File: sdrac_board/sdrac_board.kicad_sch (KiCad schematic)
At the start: 9 parts

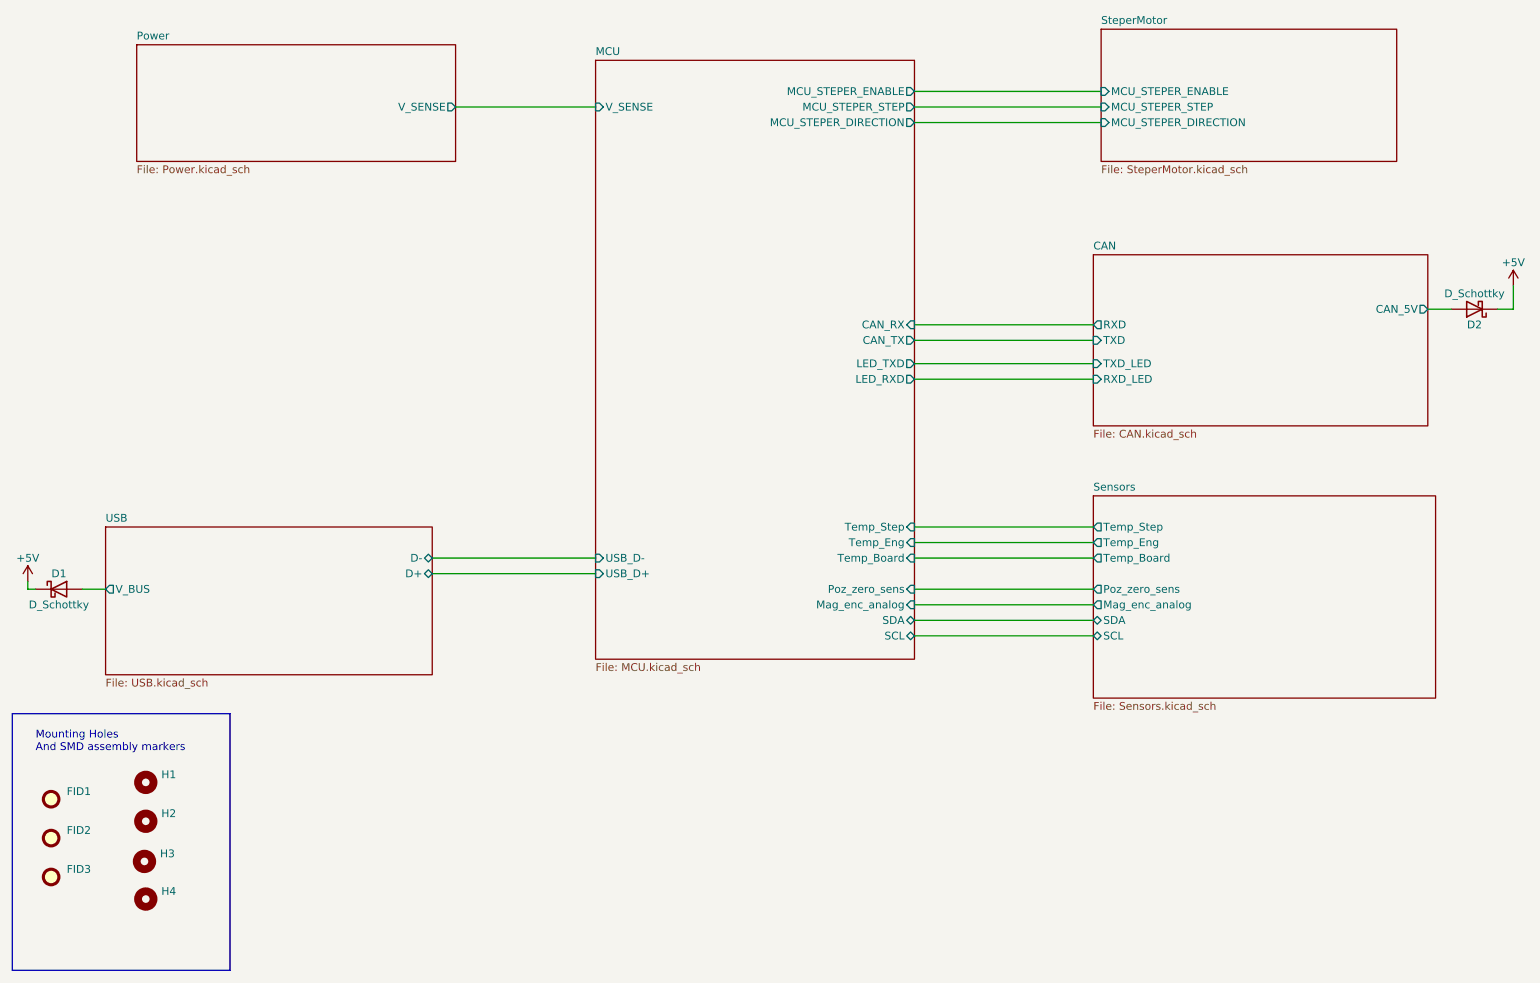
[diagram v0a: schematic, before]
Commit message: added second I2C communscation lane for synchronization and added wyas to change mcirosteping with resistors
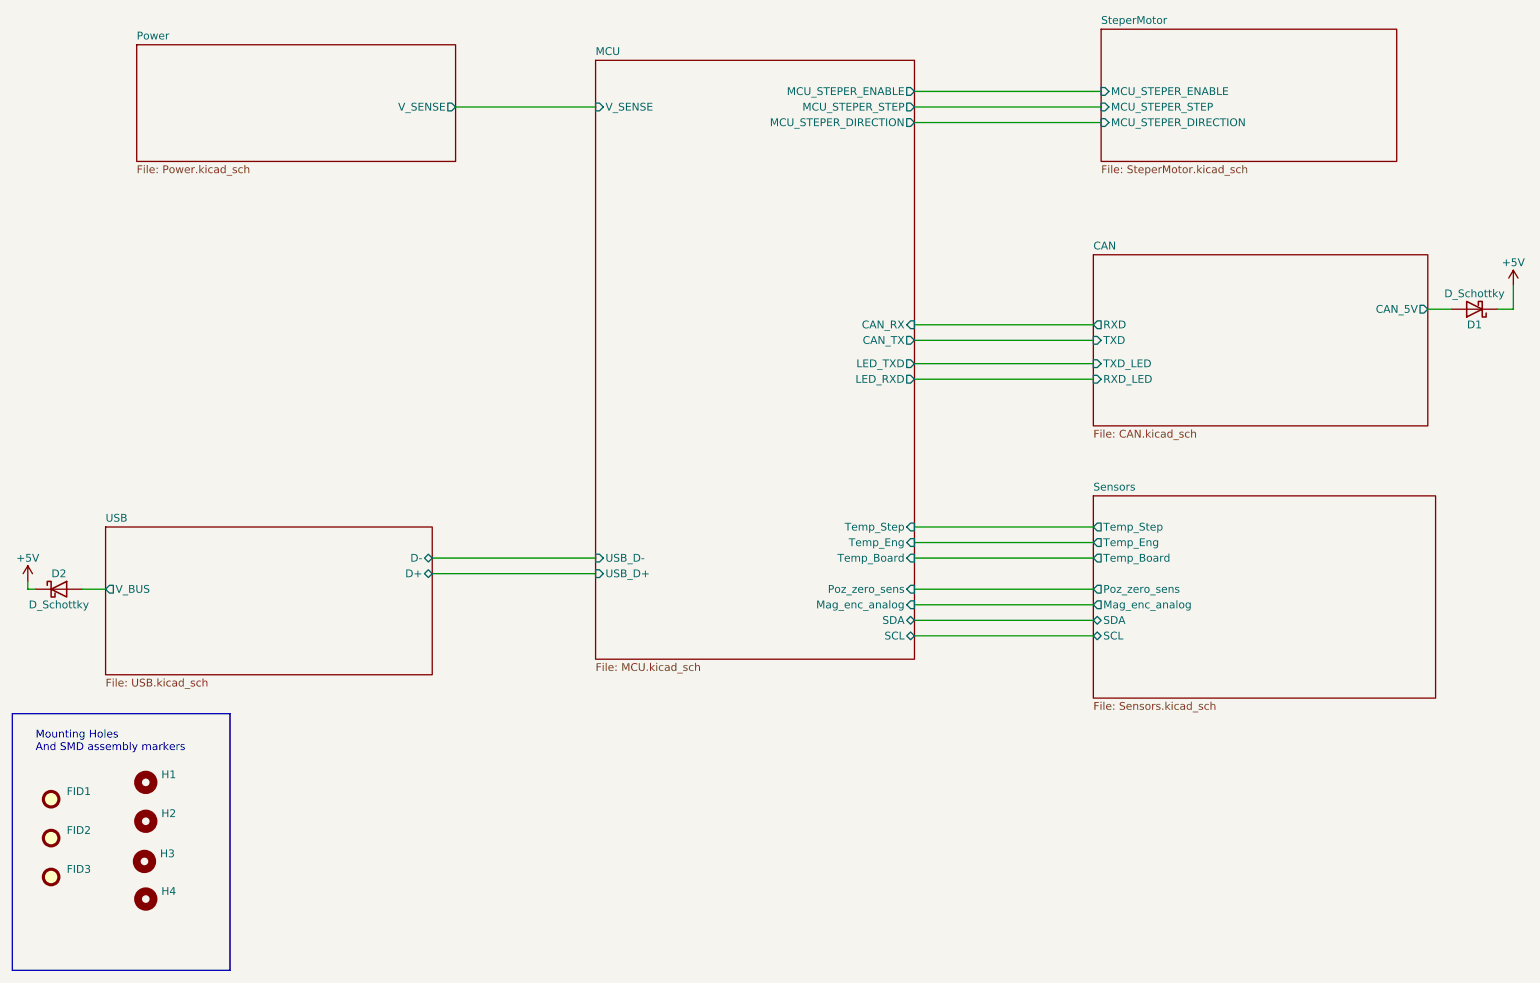
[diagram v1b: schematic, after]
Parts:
- renumbered D2 to D1, D1 to D2
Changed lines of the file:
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@@
   (symbol (lib_id "power:+5V") (at 24.13 128.27 0) (mirror y) (unit 1)
     (in_bom yes) (on_board yes) (dnp no)
-    (property "Reference" "#PWR01" (at 24.13 132.08 0)
+    (property "Reference" "#PWR02" (at 24.13 132.08 0)
       (effects (font (size 1.27 1.27)) hide)
     )
@@
       (project "sdrac_board"
         (path "/7e6d1db5-12f1-49d6-b3bd-d624ec5345e8"
-          (reference "#PWR01") (unit 1)
+          (reference "#PWR02") (unit 1)
         )
       )
@@
   (symbol (lib_id "Device:D_Schottky") (at 260.35 83.82 180) (unit 1)
     (in_bom yes) (on_board yes) (dnp no)
-    (property "Reference" "D2" (at 260.35 86.36 0)
+    (property "Reference" "D1" (at 260.35 86.36 0)
       (effects (font (size 1.27 1.27)))
     )
@@
       (project "sdrac_board"
         (path "/7e6d1db5-12f1-49d6-b3bd-d624ec5345e8"
-          (reference "D2") (unit 1)
+          (reference "D1") (unit 1)
         )
       )
@@
   (symbol (lib_id "Device:D_Schottky") (at 29.21 129.54 0) (unit 1)
     (in_bom yes) (on_board yes) (dnp no)
-    (property "Reference" "D1" (at 29.21 127 0)
+    (property "Reference" "D2" (at 29.21 127 0)
       (effects (font (size 1.27 1.27)))
     )
@@
       (project "sdrac_board"
         (path "/7e6d1db5-12f1-49d6-b3bd-d624ec5345e8"
-          (reference "D1") (unit 1)
+          (reference "D2") (unit 1)
         )
       )
@@
   (symbol (lib_id "power:+5V") (at 266.7 80.01 0) (mirror y) (unit 1)
     (in_bom yes) (on_board yes) (dnp no)
-    (property "Reference" "#PWR02" (at 266.7 83.82 0)
+    (property "Reference" "#PWR01" (at 266.7 83.82 0)
       (effects (font (size 1.27 1.27)) hide)
     )
@@
       (project "sdrac_board"
         (path "/7e6d1db5-12f1-49d6-b3bd-d624ec5345e8"
-          (reference "#PWR02") (unit 1)
+          (reference "#PWR01") (unit 1)
         )
       )

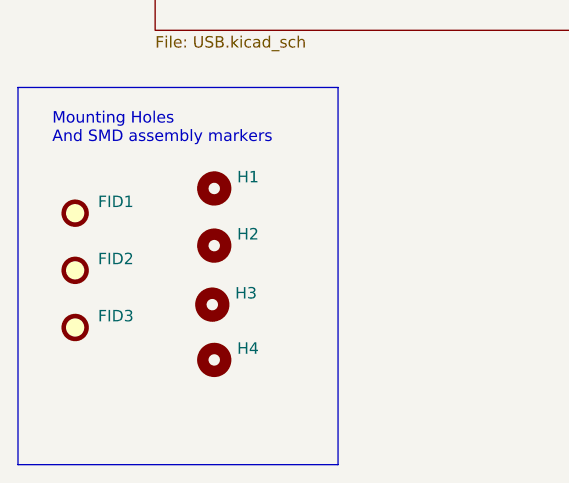
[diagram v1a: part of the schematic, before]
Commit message: added 10A screw terminal
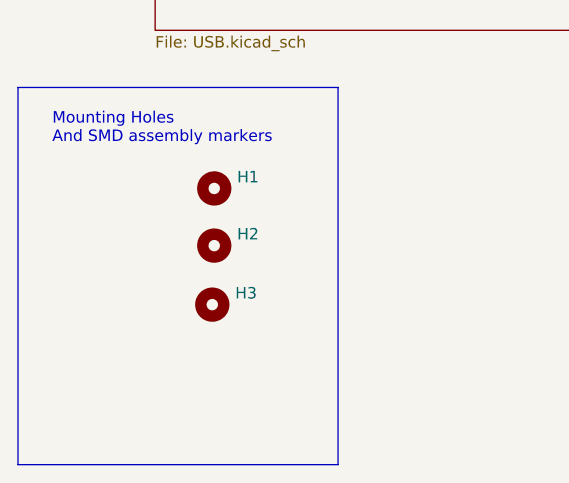
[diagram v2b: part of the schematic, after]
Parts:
- removed FID1, FID2, FID3: Fiducial, Fiducial:Fiducial_1mm_Mask2mm, symbol Mechanical:Fiducial
- removed H4: MountingHole, MountingHole:MountingHole_3.2mm_M3_ISO7380, symbol Mechanical:MountingHole
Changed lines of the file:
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@@
-    )
-  )
-  (symbol (lib_id "Mechanical:Fiducial") (at 27.94 170.18 0) (unit 1)
-    (in_bom yes) (on_board yes) (dnp no) (fields_autoplaced)
-    (property "Reference" "FID2" (at 30.48 168.91 0)
-      (effects (font (size 1.27 1.27)) (justify left))
-    )
-    (property "Value" "Fiducial" (at 30.48 171.45 0)
-      (effects (font (size 1.27 1.27)) (justify left) hide)
-    )
-    (property "Footprint" "Fiducial:Fiducial_1mm_Mask2mm" (at 27.94 170.18 0)
-      (effects (font (size 1.27 1.27)) hide)
-    )
-    (property "Datasheet" "~" (at 27.94 170.18 0)
-      (effects (font (size 1.27 1.27)) hide)
-    )
-    (instances
-      (project "sdrac_board"
-        (path "/7e6d1db5-12f1-49d6-b3bd-d624ec5345e8"
-          (reference "FID2") (unit 1)
-        )
-      )
-    )
-  )
-  (symbol (lib_id "Mechanical:Fiducial") (at 27.94 176.53 0) (unit 1)
-    (in_bom yes) (on_board yes) (dnp no) (fields_autoplaced)
-    (property "Reference" "FID3" (at 30.48 175.26 0)
-      (effects (font (size 1.27 1.27)) (justify left))
-    )
-    (property "Value" "Fiducial" (at 30.48 177.8 0)
-      (effects (font (size 1.27 1.27)) (justify left) hide)
-    )
-    (property "Footprint" "Fiducial:Fiducial_1mm_Mask2mm" (at 27.94 176.53 0)
-      (effects (font (size 1.27 1.27)) hide)
-    )
-    (property "Datasheet" "~" (at 27.94 176.53 0)
-      (effects (font (size 1.27 1.27)) hide)
-    )
-    (instances
-      (project "sdrac_board"
-        (path "/7e6d1db5-12f1-49d6-b3bd-d624ec5345e8"
-          (reference "FID3") (unit 1)
-        )
-      )
     )
   )
@@
     )
   )
-  (symbol (lib_id "Mechanical:MountingHole") (at 43.3949 180.1326 0) (unit 1)
-    (in_bom yes) (on_board yes) (dnp no) (fields_autoplaced)
-    (property "Reference" "H4" (at 45.9349 178.8626 0)
-      (effects (font (size 1.27 1.27)) (justify left))
-    )
-    (property "Value" "MountingHole" (at 45.9349 181.4026 0)
-      (effects (font (size 1.27 1.27)) (justify left) hide)
-    )
-    (property "Footprint" "MountingHole:MountingHole_3.2mm_M3_ISO7380" (at 43.3949 180.1326 0)
-      (effects (font (size 1.27 1.27)) hide)
-    )
-    (property "Datasheet" "~" (at 43.3949 180.1326 0)
-      (effects (font (size 1.27 1.27)) hide)
-    )
-    (instances
-      (project "sdrac_board"
-        (path "/7e6d1db5-12f1-49d6-b3bd-d624ec5345e8"
-          (reference "H4") (unit 1)
-        )
-      )
-    )
-  )
   (symbol (lib_id "power:+5V") (at 266.7 80.01 0) (mirror y) (unit 1)
     (in_bom yes) (on_board yes) (dnp no)
@@
         )
       )
-    )
-  )
-  (symbol (lib_id "Mechanical:Fiducial") (at 27.94 163.83 0) (unit 1)
-    (in_bom yes) (on_board yes) (dnp no) (fields_autoplaced)
-    (property "Reference" "FID1" (at 30.48 162.56 0)
-      (effects (font (size 1.27 1.27)) (justify left))
-    )
-    (property "Value" "Fiducial" (at 30.48 165.1 0)
-      (effects (font (size 1.27 1.27)) (justify left) hide)
-    )
-    (property "Footprint" "Fiducial:Fiducial_1mm_Mask2mm" (at 27.94 163.83 0)
-      (effects (font (size 1.27 1.27)) hide)
-    )
-    (property "Datasheet" "~" (at 27.94 163.83 0)
-      (effects (font (size 1.27 1.27)) hide)
-    )
-    (instances
-      (project "sdrac_board"
-        (path "/7e6d1db5-12f1-49d6-b3bd-d624ec5345e8"
-          (reference "FID1") (unit 1)
-        )
-      )
